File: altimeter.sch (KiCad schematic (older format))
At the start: 25 parts, among them J101 USB_B_Micro, Q101 Q_PMOS_DGS, U101 STM32F302CCTx, U102 MS5611-01BA, U103 MIC5219-3.3YM5, U104 LF50_TO252, U105 OPAMP, U106 MT25Q, U107 AIS2120SXTR, Y101 Crystal_Small

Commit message: updates to schematic
Signed-off-by: Thomas Schmid <tom@binary-kitchen.de>
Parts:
- Y101: footprint Crystal:Crystal_SMD_HC49-SD -> Crystal:Crystal_SMD_5032-2Pin_5.0x3.2mm_HandSoldering
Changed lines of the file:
@@
 F 0 "Y101" V 1300 2238 50  0000 L CNN
 F 1 "Crystal_Small" V 1345 2238 50  0001 L CNN
-F 2 "Crystal:Crystal_SMD_HC49-SD" H 1300 2150 50  0001 C CNN
+F 2 "Crystal:Crystal_SMD_5032-2Pin_5.0x3.2mm_HandSoldering" H 1300 2150 50  0001 C CNN
 F 3 "~" H 1300 2150 50  0001 C CNN
 	1    1300 2150

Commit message: add pyro output stages
Signed-off-by: Thomas Schmid <tom@binary-kitchen.de>
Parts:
- removed J101: USB_B_Micro, Connector_USB:USB_Micro-B_Molex-105017-0001, symbol Connector:USB_B_Micro
- removed R105: 1.5k, Resistor_SMD:R_0603_1608Metric_Pad1.05x0.95mm_HandSolder, symbol Device:R_Small
- R103, R104: value R_Small -> 100k
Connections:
- net labels added: ARM_LOW, FIRE_PYRO1, FIRE_PYRO2, FIRE_PYRO3, PYRO1_HIGH, PYRO1_LOW, PYRO2_HIGH, PYRO2_LOW, PYRO2_SENSE, PYRO3_HIGH, PYRO3_LOW, PYRO3_SENSE, PYRO_TEST_ENABLE, VBAT_SENSE
- net labels removed: PWM1, PYRO1
- wire segments 96 -> 99
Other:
- note added: "5V Source Selector"
- note added: "Pyro output and test circuit"
- moved on the sheet: C103, C104, C105, C106, C107, C108, D101, D102, Q101, R101, R102, R103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

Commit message: update pyro output stage. add a fuse to the test circuit and remove pullup for sense line
Signed-off-by: Thomas Schmid <tom@binary-kitchen.de>
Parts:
- removed U105: OPAMP, symbol pspice:OPAMP
- added U106: LM397, Package_TO_SOT_SMD:SOT-23-5_HandSoldering, symbol altimeter:LM397
- Q101: value Q_PMOS_DGS -> DMG2301L; footprint (none) -> Package_TO_SOT_SMD:SOT-23
- R101, R102, R103, R104: footprint Resistor_SMD:R_0603_1608Metric_Pad1.05x0.95mm_HandSolder -> Resistor_SMD:R_0402_1005Metric
- renumbered C108 to C103, C103 to C104, C104 to C105, C107 to C106, C105 to C107, C106 to C108, U106 to U102, U107 to U103, U103 to U104, U104 to U105, U102 to U107
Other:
- moved on the sheet: C104, C105, C107, C108, Q101, R103, R104, U102, U104, U105

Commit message: more work on schematic and layout
Signed-off-by: Thomas Schmid <tom@lfence.de>
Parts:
- removed U106: LM397, Package_TO_SOT_SMD:SOT-23-5_HandSoldering, symbol altimeter:LM397
- removed Y101: Crystal_Small, Crystal:Crystal_SMD_5032-2Pin_5.0x3.2mm_HandSoldering, symbol Device:Crystal_Small
- added C1, C2: 100n, symbol Device:C_Small
- added C3: CP, Capacitor_THT:CP_Axial_L11.0mm_D8.0mm_P15.00mm_Horizontal, symbol Device:CP
- added U1: LMV331, symbol Comparator:LMV331
- added Y1: Crystal_GND24, Crystal:Crystal_SMD_2520-4Pin_2.5x2.0mm, symbol Device:Crystal_GND24
- C101, C102: value C_Small -> 22p
- C103: value C_Small -> 1u
- C104: value C_Small -> 100n; footprint Capacitor_SMD:C_0603_1608Metric_Pad1.05x0.95mm_HandSolder -> Capacitor_SMD:C_0805_2012Metric_Pad1.15x1.40mm_HandSolder
- C107: value C_Small -> 2.2u
- R101, R102: value R -> 680
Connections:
- net +3V3: now also C1.2, C2.2, U1.3 (-)
- net +5V: now also U1.5 (V+)
- net +BATT: now also C3.1
- net GND: now also C1.1, C2.1, C3.2, U1.2 (V-), Y1.2, Y1.4
- net at C101.1, U101.3 (PC14): now also Y1.1
- net at C102.1, U101.4 (PC15): now also Y1.3
- net at Q101.2 (G): now also U1.4
- net at R103.2, R104.1: now also U1.1 (+)
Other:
- moved on the sheet: C101, C102, D101, D102, R101, R102

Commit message: update
Signed-off-by: Thomas Schmid <tom@lfence.de>
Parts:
- C101, C102: footprint Capacitor_SMD:C_0603_1608Metric_Pad1.05x0.95mm_HandSolder -> Capacitor_SMD:C_0402_1005Metric
- C103: footprint (none) -> Capacitor_SMD:C_0603_1608Metric_Pad1.05x0.95mm_HandSolder
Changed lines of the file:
@@
 F 0 "C101" V 771 1950 50  0000 C CNN
 F 1 "22p" V 862 1950 50  0000 C CNN
-F 2 "Capacitor_SMD:C_0603_1608Metric_Pad1.05x0.95mm_HandSolder" H 1000 1950 50  0001 C CNN
+F 2 "Capacitor_SMD:C_0402_1005Metric" H 1000 1950 50  0001 C CNN
 F 3 "~" H 1000 1950 50  0001 C CNN
 	1    1000 1950
@@
 F 0 "C102" V 1137 2350 50  0000 C CNN
 F 1 "22p" V 1228 2350 50  0000 C CNN
-F 2 "Capacitor_SMD:C_0603_1608Metric_Pad1.05x0.95mm_HandSolder" H 1000 2350 50  0001 C CNN
+F 2 "Capacitor_SMD:C_0402_1005Metric" H 1000 2350 50  0001 C CNN
 F 3 "~" H 1000 2350 50  0001 C CNN
 	1    1000 2350
@@
 F 0 "C103" V 8021 5150 50  0000 C CNN
 F 1 "1u" V 8112 5150 50  0000 C CNN
-F 2 "" H 8250 5150 50  0001 C CNN
+F 2 "Capacitor_SMD:C_0603_1608Metric_Pad1.05x0.95mm_HandSolder" H 8250 5150 50  0001 C CNN
 F 3 "~" H 8250 5150 50  0001 C CNN
 	1    8250 5150

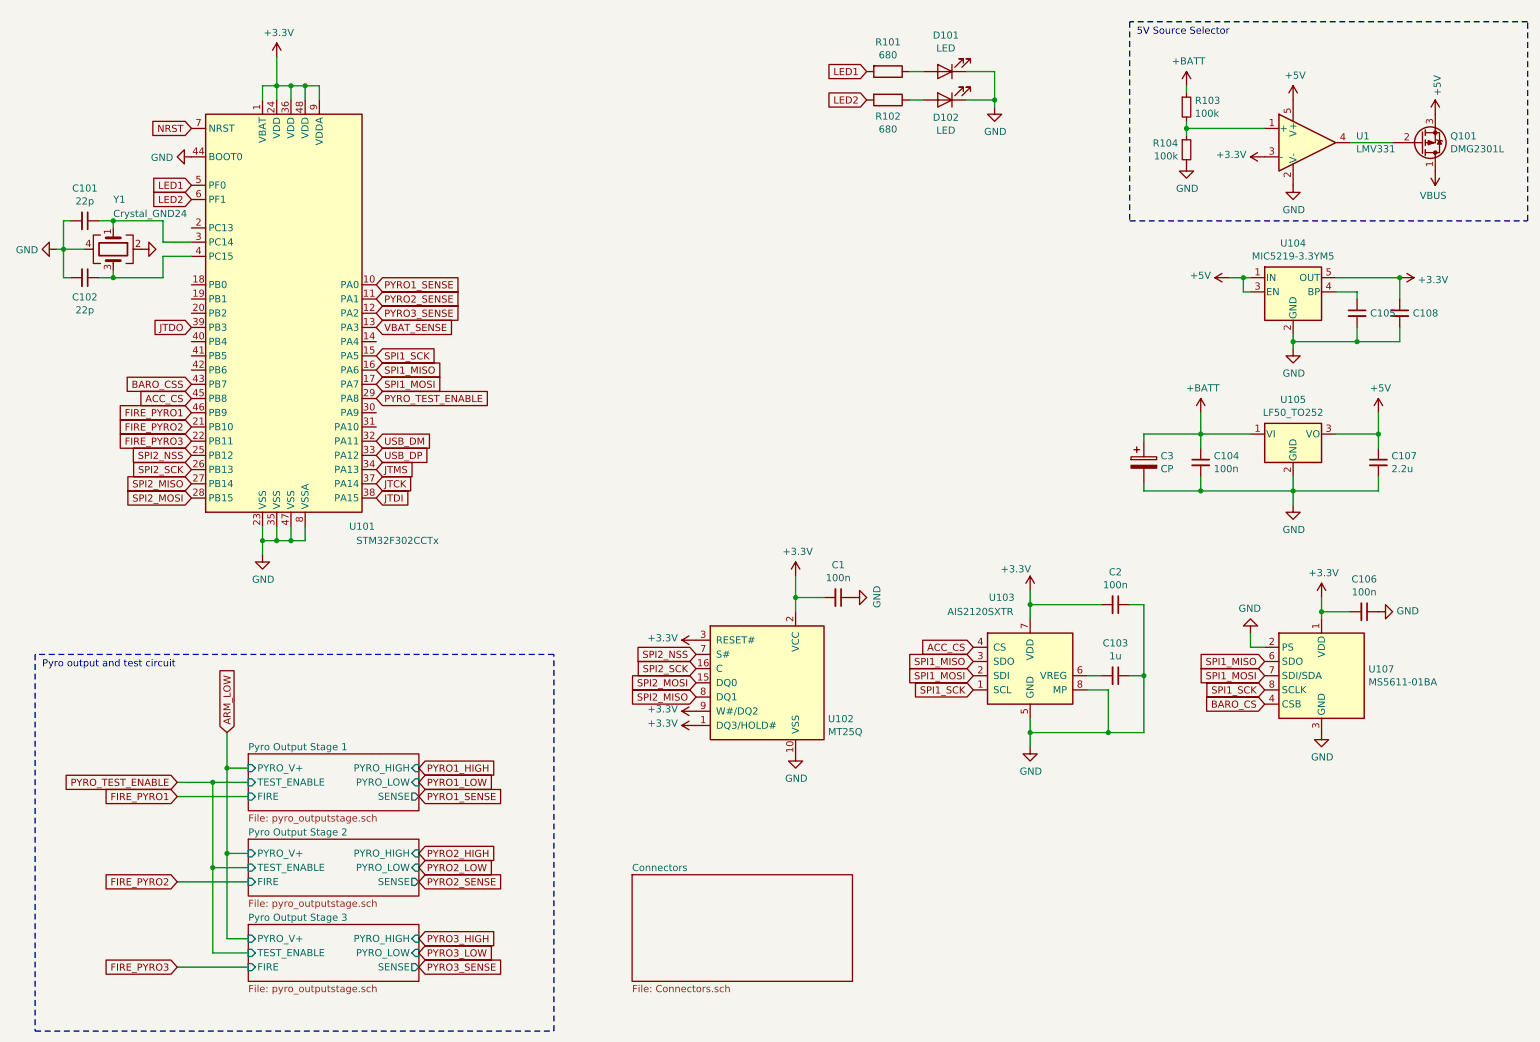
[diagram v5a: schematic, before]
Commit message: update to schematic and layout
Signed-off-by: Thomas Schmid <tom@lfence.de>
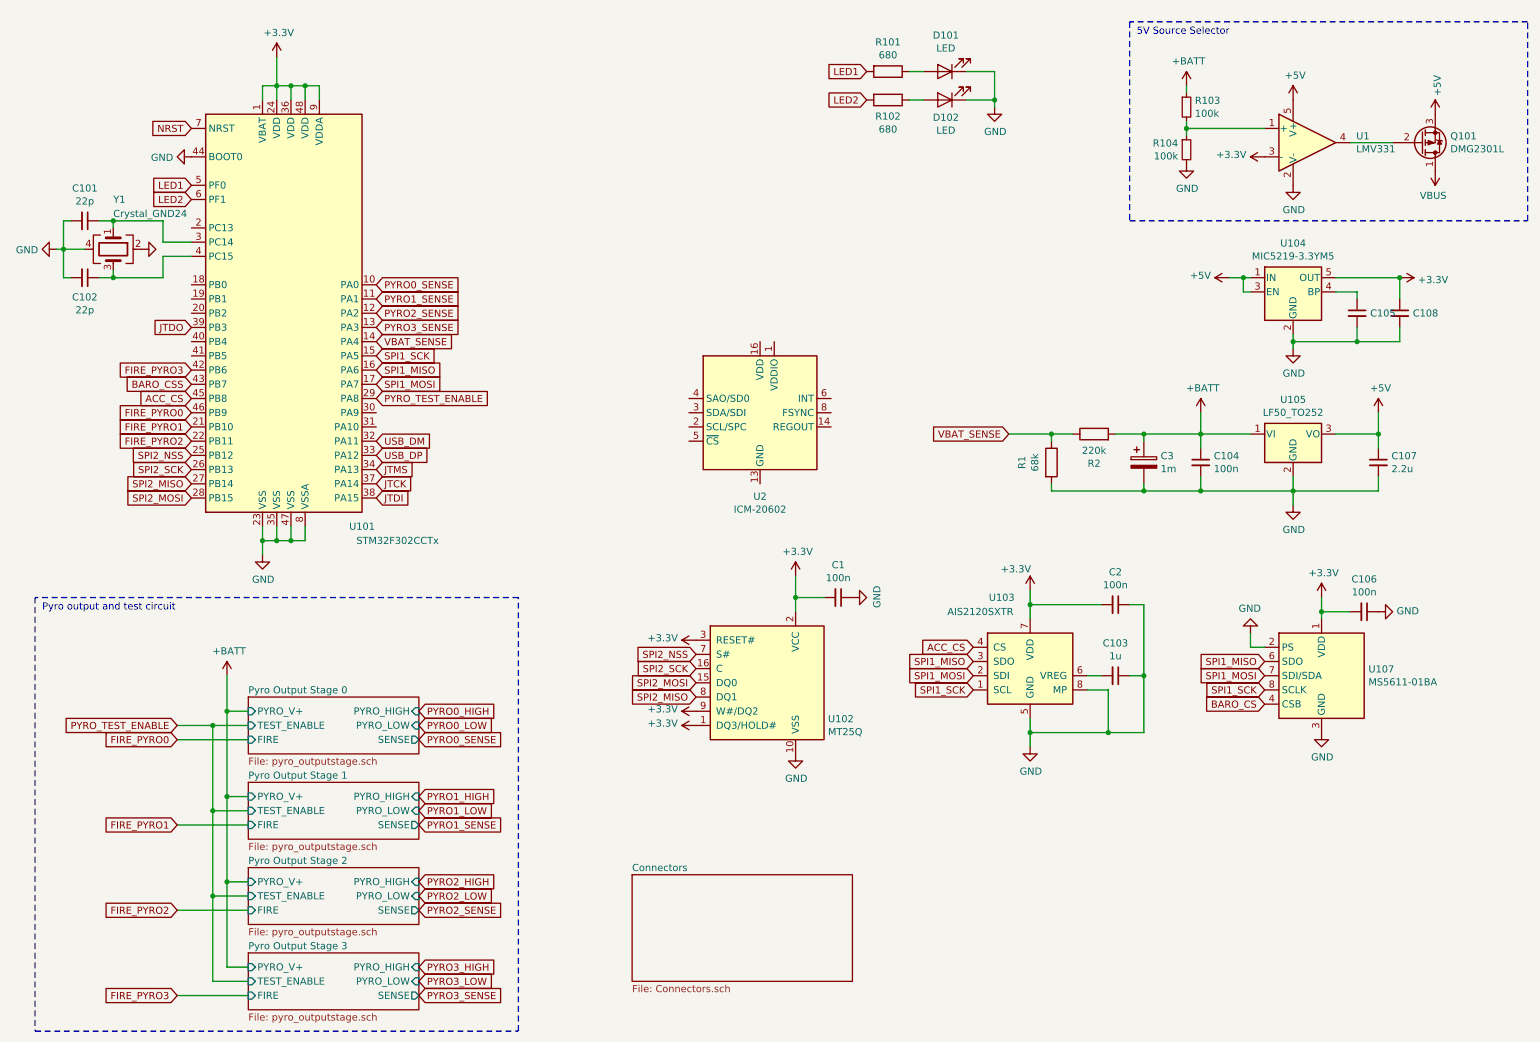
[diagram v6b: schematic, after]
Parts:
- added R1: 68k, Resistor_SMD:R_0402_1005Metric, symbol Device:R
- added R2: 220k, Resistor_SMD:R_0402_1005Metric, symbol Device:R
- added U2: ICM-20602, Package_LGA:LGA-16_3x3mm_P0.5mm_LayoutBorder3x5y, symbol Sensor_Motion:ICM-20602
- C3: value CP -> 1m
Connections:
- net +BATT: now also R2.2
- net FIRE_PYRO1: now also U101.21 (PB10); no longer U101.46 (PB9)
- net FIRE_PYRO2: now also U101.22 (PB11); no longer U101.21 (PB10)
- net FIRE_PYRO3: now also U101.42 (PB6); no longer U101.22 (PB11)
- net GND: now also R1.2
- net PYRO1_SENSE: now also U101.11 (PA1); no longer U101.10 (PA0)
- net PYRO2_SENSE: now also U101.12 (PA2); no longer U101.11 (PA1)
- net PYRO3_SENSE: now also U101.13 (PA3); no longer U101.12 (PA2)
- net VBAT_SENSE: now also U101.14 (PA4), R1.1, R2.1; no longer U101.13 (PA3)
- new net: U2.10 (GND), U2.11 (GND), U2.12 (GND), U2.13 (GND), U2.15 (GND), U2.9 (GND)
- new net FIRE_PYRO0: U101.46 (PB9)
- new net PYRO0_SENSE: U101.10 (PA0)
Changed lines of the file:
@@
 $Descr A4 11693 8268
 encoding utf-8
-Sheet 1 5
+Sheet 1 6
 Title ""
 Date ""
@@
 	9500 3850 10100 3850
 $Sheet
-S 2150 5700 1200 400
+S 2150 5300 1200 400
 U 5D473C9B
+F0 "Pyro Output Stage 0" 50
+F1 "pyro_outputstage.sch" 50
+F2 "TEST_ENABLE" I L 2150 5500 50
+F3 "PYRO_LOW" I R 3350 5500 50
+F4 "PYRO_HIGH" I R 3350 5400 50
+F5 "PYRO_V+" I L 2150 5400 50
+F6 "FIRE" I L 2150 5600 50
+F7 "SENSE" O R 3350 5600 50
+$EndSheet
+$Sheet
+S 2150 5900 1200 400
+U 5D488E46
 F0 "Pyro Output Stage 1" 50
 F1 "pyro_outputstage.sch" 50
-F2 "TEST_ENABLE" I L 2150 5900 50
-F3 "PYRO_LOW" I R 3350 5900 50
-F4 "PYRO_HIGH" I R 3350 5800 50
-F5 "PYRO_V+" I L 2150 5800 50
-F6 "FIRE" I L 2150 6000 50
-F7 "SENSE" O R 3350 6000 50
+F2 "TEST_ENABLE" I L 2150 6100 50
+F3 "PYRO_LOW" I R 3350 6100 50
+F4 "PYRO_HIGH" I R 3350 6000 50
+F5 "PYRO_V+" I L 2150 6000 50
+F6 "FIRE" I L 2150 6200 50
+F7 "SENSE" O R 3350 6200 50
 $EndSheet
 $Sheet
-S 2150 6300 1200 400
-U 5D488E46
+S 2150 6500 1200 400
+U 5D48B429
 F0 "Pyro Output Stage 2" 50
 F1 "pyro_outputstage.sch" 50
-F2 "TEST_ENABLE" I L 2150 6500 50
-F3 "PYRO_LOW" I R 3350 6500 50
-F4 "PYRO_HIGH" I R 3350 6400 50
-F5 "PYRO_V+" I L 2150 6400 50
-F6 "FIRE" I L 2150 6600 50
-F7 "SENSE" O R 3350 6600 50
+F2 "TEST_ENABLE" I L 2150 6700 50
+F3 "PYRO_LOW" I R 3350 6700 50
+F4 "PYRO_HIGH" I R 3350 6600 50
+F5 "PYRO_V+" I L 2150 6600 50
+F6 "FIRE" I L 2150 6800 50
+F7 "SENSE" O R 3350 6800 50
 $EndSheet
-$Sheet
-S 2150 6900 1200 400
-U 5D48B429
-F0 "Pyro Output Stage 3" 50
-F1 "pyro_outputstage.sch" 50
-F2 "TEST_ENABLE" I L 2150 7100 50
-F3 "PYRO_LOW" I R 3350 7100 50
-F4 "PYRO_HIGH" I R 3350 7000 50
-F5 "PYRO_V+" I L 2150 7000 50
-F6 "FIRE" I L 2150 7200 50
-F7 "SENSE" O R 3350 7200 50
-$EndSheet
-Text GLabel 2000 5550 1    50   Input ~ 0
-ARM_LOW
-Wire Wire Line
-	2000 5550 2000 5800
-Wire Wire Line
-	2000 5800 2150 5800
-Wire Wire Line
-	2150 6400 2000 6400
-Wire Wire Line
-	2000 6400 2000 5800
-Connection ~ 2000 5800
-Wire Wire Line
-	2150 7000 2000 7000
-Wire Wire Line
-	2000 7000 2000 6400
-Connection ~ 2000 6400
-Text GLabel 1650 5900 0    50   Input ~ 0
+Wire Wire Line
+	2000 5400 2150 5400
+Wire Wire Line
+	2150 6000 2000 6000
+Wire Wire Line
+	2000 6000 2000 5400
+Connection ~ 2000 5400
+Wire Wire Line
+	2150 6600 2000 6600
+Wire Wire Line
+	2000 6600 2000 6000
+Connection ~ 2000 6000
+Text GLabel 1650 5500 0    50   Input ~ 0
 PYRO_TEST_ENABLE
 Wire Wire Line
-	1650 5900 1900 5900
-Wire Wire Line
-	2150 6500 1900 6500
-Wire Wire Line
-	1900 6500 1900 5900
-Connection ~ 1900 5900
-Wire Wire Line
-	1900 5900 2150 5900
-Wire Wire Line
-	2150 7100 1900 7100
-Wire Wire Line
-	1900 7100 1900 6500
-Connection ~ 1900 6500
-Text GLabel 1650 6000 0    50   Input ~ 0
+	1650 5500 1900 5500
+Wire Wire Line
+	2150 6100 1900 6100
+Wire Wire Line
+	1900 6100 1900 5500
+Connection ~ 1900 5500
+Wire Wire Line
+	1900 5500 2150 5500
+Wire Wire Line
+	2150 6700 1900 6700
+Wire Wire Line
+	1900 6700 1900 6100
+Connection ~ 1900 6100
+Text GLabel 1650 5600 0    50   Input ~ 0
+FIRE_PYRO0
+Text GLabel 1650 6200 0    50   Input ~ 0
 FIRE_PYRO1
-Text GLabel 1650 6600 0    50   Input ~ 0
+Text GLabel 1650 6800 0    50   Input ~ 0
 FIRE_PYRO2
-Text GLabel 1650 7200 0    50   Input ~ 0
-FIRE_PYRO3
-Wire Wire Line
-	1650 7200 2150 7200
-Wire Wire Line
-	1650 6600 2150 6600
-Wire Wire Line
-	1650 6000 2150 6000
-Text GLabel 3350 5900 2    50   Input ~ 0
+Wire Wire Line
+	1650 6800 2150 6800
+Wire Wire Line
+	1650 6200 2150 6200
+Wire Wire Line
+	1650 5600 2150 5600
+Text GLabel 3350 6100 2    50   Input ~ 0
 PYRO1_LOW
-Text GLabel 3350 5800 2    50   Input ~ 0
-PYRO1_HIGH
-Text GLabel 3350 6400 2    50   Input ~ 0
+Text GLabel 3350 6600 2    50   Input ~ 0
 PYRO2_HIGH
-Text GLabel 3350 7000 2    50   Input ~ 0
+Text GLabel 3350 7200 2    50   Input ~ 0
 PYRO3_HIGH
-Text GLabel 3350 6500 2    50   Input ~ 0
+Text GLabel 3350 6700 2    50   Input ~ 0
 PYRO2_LOW
-Text GLabel 3350 7100 2    50   Input ~ 0
+Text GLabel 3350 7300 2    50   Input ~ 0
 PYRO3_LOW
-Text GLabel 3350 6000 2    50   Input ~ 0
+Text GLabel 3350 6200 2    50   Input ~ 0
 PYRO1_SENSE
-Text GLabel 3350 6600 2    50   Input ~ 0
+Text GLabel 3350 6800 2    50   Input ~ 0
 PYRO2_SENSE
-Text GLabel 3350 7200 2    50   Input ~ 0
+Text GLabel 3350 7400 2    50   Input ~ 0
 PYRO3_SENSE
 Text GLabel 3050 3200 2    50   Input ~ 0
 PYRO_TEST_ENABLE
 Text GLabel 1750 3300 0    50   Input ~ 0
+FIRE_PYRO0
+Text GLabel 1750 3400 0    50   Input ~ 0
 FIRE_PYRO1
-Text GLabel 1750 3400 0    50   Input ~ 0
+Text GLabel 1750 3500 0    50   Input ~ 0
 FIRE_PYRO2
-Text GLabel 1750 3500 0    50   Input ~ 0
-FIRE_PYRO3
 Text GLabel 3050 2400 2    50   Input ~ 0
+PYRO0_SENSE
+Text GLabel 3050 2500 2    50   Input ~ 0
 PYRO1_SENSE
-Text GLabel 3050 2500 2    50   Input ~ 0
+Text GLabel 3050 2600 2    50   Input ~ 0
 PYRO2_SENSE
-Text GLabel 3050 2600 2    50   Input ~ 0
-PYRO3_SENSE
-Text GLabel 3050 2700 2    50   Input ~ 0
+Text GLabel 3050 2800 2    50   Input ~ 0
 VBAT_SENSE
-Wire Notes Line
-	650  5000 650  7650
-Wire Notes Line
-	650  7650 4300 7650
-Wire Notes Line
-	4300 7650 4300 5000
-Wire Notes Line
-	4300 5000 650  5000
-Text Notes 700  5100 0    50   ~ 0
+Text Notes 700  4700 0    50   ~ 0
 Pyro output and test circuit
 $Comp
@@
 P 8450 3650
 F 0 "C3" H 8568 3696 50  0000 L CNN
-F 1 "CP" H 8568 3605 50  0000 L CNN
+F 1 "1m" H 8568 3605 50  0000 L CNN
 F 2 "Capacitor_THT:CP_Axial_L11.0mm_D8.0mm_P15.00mm_Horizontal" H 8488 3500 50  0001 C CNN
 F 3 "~" H 8450 3650 50  0001 C CNN
@@
 	0    -1   -1   0
 $EndComp
+$Comp
+L Device:R R2
+U 1 1 5D4C5890
+P 8100 3450
+F 0 "R2" V 7893 3450 50  0000 C CNN
+F 1 "220k" V 7984 3450 50  0000 C CNN
+F 2 "Resistor_SMD:R_0402_1005Metric" V 8030 3450 50  0001 C CNN
+F 3 "~" H 8100 3450 50  0001 C CNN
+	1    8100 3450
+	0    -1   -1   0
+$EndComp
+$Comp
+L Device:R R1
+U 1 1 5D4C75D7
+P 7800 3650
+F 0 "R1" V 7593 3650 50  0000 C CNN
+F 1 "68k" V 7684 3650 50  0000 C CNN
+F 2 "Resistor_SMD:R_0402_1005Metric" V 7730 3650 50  0001 C CNN
+F 3 "~" H 7800 3650 50  0001 C CNN
+	1    7800 3650
+	1    0    0    -1
+$EndComp
+Wire Wire Line
+	7800 3800 7800 3850
+Wire Wire Line
+	7800 3850 8450 3850
+Connection ~ 8450 3850
+Wire Wire Line
+	7800 3500 7800 3450
+Wire Wire Line
+	7800 3450 7950 3450
+Wire Wire Line
+	8250 3450 8450 3450
+Connection ~ 8450 3450
+Wire Wire Line
+	7800 3450 7500 3450
+Connection ~ 7800 3450
+Text GLabel 7500 3450 0    50   Input ~ 0
+VBAT_SENSE
+$Sheet
+S 2150 7100 1200 400
+U 5D4E7D5B
+F0 "Pyro Output Stage 3" 50
+F1 "pyro_outputstage.sch" 50
+F2 "TEST_ENABLE" I L 2150 7300 50
+F3 "PYRO_LOW" I R 3350 7300 50
+F4 "PYRO_HIGH" I R 3350 7200 50
+F5 "PYRO_V+" I L 2150 7200 50
+F6 "FIRE" I L 2150 7400 50
+F7 "SENSE" O R 3350 7400 50
+$EndSheet
+Wire Wire Line
+	2000 6600 2000 7200
+Connection ~ 2000 6600
+Wire Wire Line
+	2150 7200 2000 7200
+Wire Wire Line
+	1900 7300 1900 6700
+Connection ~ 1900 6700
+Text GLabel 1650 7400 0    50   Input ~ 0
+FIRE_PYRO3
+Text GLabel 3350 6000 2    50   Input ~ 0
+PYRO1_HIGH
+Text GLabel 3350 5500 2    50   Input ~ 0
+PYRO0_LOW
+Text GLabel 3350 5600 2    50   Input ~ 0
+PYRO0_SENSE
+Text GLabel 3050 2700 2    50   Input ~ 0
+PYRO3_SENSE
+Text GLabel 1750 3000 0    50   Input ~ 0
+FIRE_PYRO3
+Wire Notes Line
+	650  4600 650  7650
+Wire Notes Line
+	650  7650 4050 7650
+Wire Notes Line
+	4050 7650 4050 4600
+Wire Notes Line
+	4050 4600 650  4600
+Wire Wire Line
+	1900 7300 2150 7300
+Wire Wire Line
+	1650 7400 2150 7400
+Text GLabel 3350 5400 2    50   Input ~ 0
+PYRO0_HIGH
+Wire Wire Line
+	2000 5150 2000 5400
+$Comp
+L power:+BATT #PWR0132
+U 1 1 5D50022D
+P 2000 5150
+F 0 "#PWR0132" H 2000 5000 50  0001 C CNN
+F 1 "+BATT" H 2015 5323 50  0000 C CNN
+F 2 "" H 2000 5150 50  0001 C CNN
+F 3 "" H 2000 5150 50  0001 C CNN
+	1    2000 5150
+	1    0    0    -1
+$EndComp
+$Comp
+L Sensor_Motion:ICM-20602 U2
+U 1 1 5D54A91F
+P 5750 3300
+F 0 "U2" H 5750 2711 50  0000 C CNN
+F 1 "ICM-20602" H 5750 2620 50  0000 C CNN
+F 2 "Package_LGA:LGA-16_3x3mm_P0.5mm_LayoutBorder3x5y" H 5750 3550 50  0001 C CNN
+F 3 "http://www.invensense.com/wp-content/uploads/2016/10/DS-000176-ICM-20602-v1.0.pdf" H 5800 4250 50  0001 C CNN
+	1    5750 3300
+	1    0    0    -1
+$EndComp
 $EndSCHEMATC

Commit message: more work on schematic and layout
Signed-off-by: Thomas Schmid <tom@binary-kitchen.de>
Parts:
- removed D102: LED, LED_SMD:LED_0603_1608Metric, symbol Device:LED
- removed R102: 680, Resistor_SMD:R_0402_1005Metric, symbol Device:R
- removed U2: ICM-20602, Package_LGA:LGA-16_3x3mm_P0.5mm_LayoutBorder3x5y, symbol Sensor_Motion:ICM-20602
- added C? (x2): 100n, symbol Device:C_Small
- added D103: 1N4148WS, Diode_SMD:D_SOD-323, symbol Diode:1N4148WS
- added LS101: Speaker_Crystal, altimeter:CSS-95B30-SMT, symbol Device:Speaker_Crystal
- added Q102: DMG2301L, Package_TO_SOT_SMD:SOT-23, symbol Device:Q_PMOS_DGS
- added U?: BMI088, symbol altimeter:BMI088
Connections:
- net +3V3: now also C?.2, U?.3 (VDD)
- net +5V: now also D103.1 (K), LS101.1
- net ACC_CS: now also U101.21 (PB10); no longer U101.45 (PB8)
- net BARO_CSS: now also U101.20 (PB2); no longer U101.43 (PB7)
- net FIRE_PYRO0: now also U101.40 (PB4); no longer U101.46 (PB9)
- net FIRE_PYRO1: now also U101.41 (PB5); no longer U101.21 (PB10)
- net FIRE_PYRO2: now also U101.42 (PB6); no longer U101.22 (PB11)
- net FIRE_PYRO3: now also U101.43 (PB7); no longer U101.42 (PB6)
- net GND: now also C?.1, C?.1, Q102.1 (D), U?.2 (NC), U?.4 (GNDA), U?.6 (GNDIO), U?.7 (PS)
- net SPI1_MISO: now also U?.10 (SDO2), U?.15 (SDO1)
- net SPI1_MOSI: now also U?.9 (SDA/SDI)
- net SPI1_SCK: now also U?.8 (SCL/SCK)
- net IMU_GYRO_CS: now reaches U101.18 (PB0)
- net IMU_GYRO_CS: now also U?.5 (CSB2)
- net SUMMER: now reaches U101.19 (PB1)
- net SUMMER: now also Q102.2 (G)
- net UART1_TX: now reaches U101.30 (PA9)
- net UART1_RX: now reaches U101.31 (PA10)
- net JTCK renamed SWCLK
- net JTDI renamed INT1
- net INT1: now also U?.16 (INT1)
- net JTMS renamed SWDIO
- net LED2 renamed INT2
- net INT2: now also U?.12 (INT3)
- net USB_DM renamed USB_D_N
- net USB_DP renamed USB_D_P
- new net: D103.2 (A), LS101.2, Q102.3 (S)
- new net: C?.2, U?.11 (VDDIO)
- new net IMU_ACC_CS: U101.22 (PB11), U?.14 (CSB1)
- new net PWM1: U101.45 (PB8)
- new net PWM2: U101.46 (PB9)
- no-connect marks 0 -> 2
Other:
- moved on the sheet: C101, C102, C104, C105, C107, C108, C3, D101, R1, R101, R2, U104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

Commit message: flash considerations
Signed-off-by: Thomas Schmid <thomas.schmid@engeex.de>
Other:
- note added: "Replace Flash with JEDEC compatible flash for zephyr compatibility"
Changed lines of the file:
@@
 Text GLabel 1750 1800 0    50   Input ~ 0
 INT2
+Text Notes 4450 6000 0    50   ~ 0
+Replace Flash with JEDEC compatible flash for zephyr compatibility
 $EndSCHEMATC
